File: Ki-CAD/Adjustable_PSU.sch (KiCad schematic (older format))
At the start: 12 parts, among them T1 TRANSFO4 - 50V

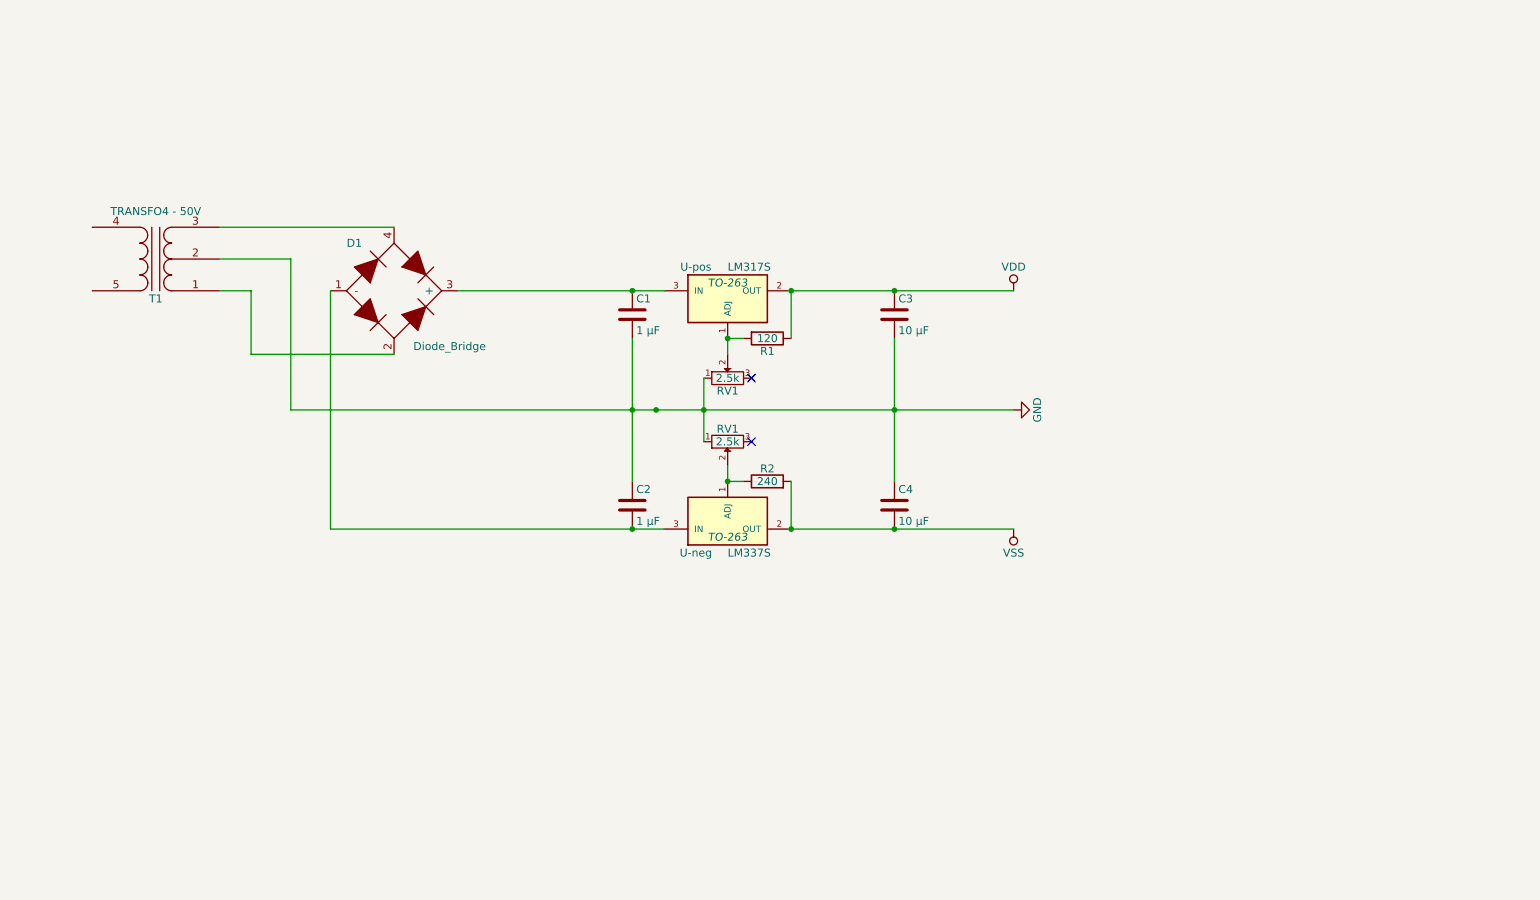
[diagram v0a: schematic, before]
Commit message: added 5v rail and new footprints (to be added to future personal kicad repo)
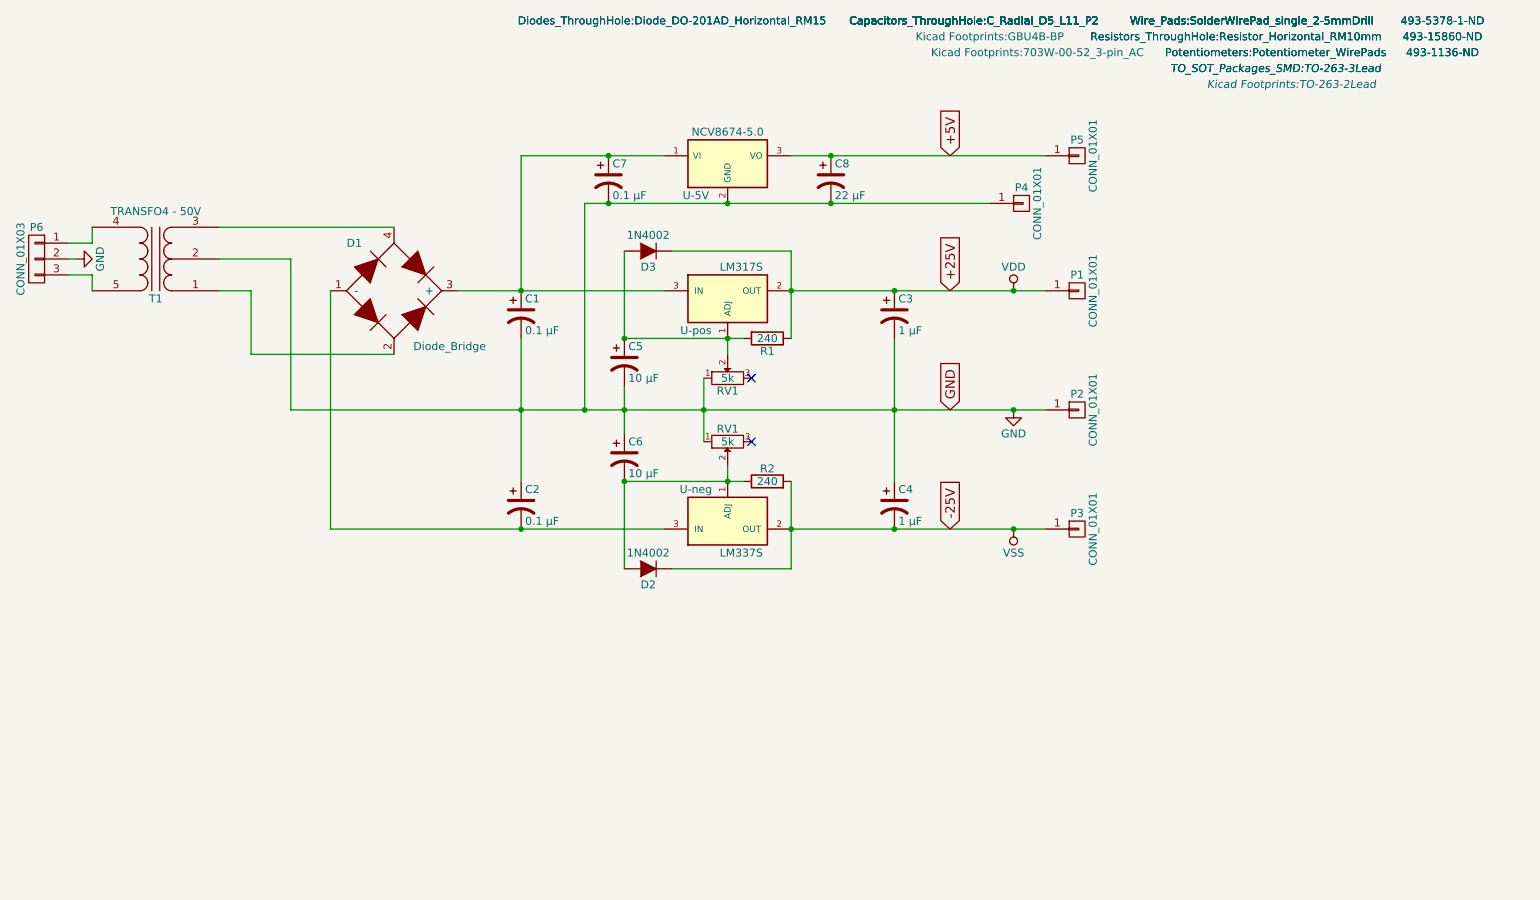
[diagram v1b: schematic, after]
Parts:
- removed C1, C2: 1 μF, symbol C
- removed C3, C4: 10 μF, symbol C
- added C1, C2, C7: 0.1 μF, Capacitors_ThroughHole:C_Radial_D5_L11_P2, symbol CP1
- added C3, C4: 1 μF, Capacitors_ThroughHole:C_Radial_D5_L11_P2, symbol CP1
- added C5, C6: 10 μF, Capacitors_ThroughHole:C_Radial_D5_L11_P2, symbol CP1
- added C8: 22 μF, Capacitors_ThroughHole:C_Radial_D5_L11_P2, symbol CP1
- added D2, D3: 1N4002, Diodes_ThroughHole:Diode_DO-201AD_Horizontal_RM15, symbol D
- added P1, P2, P3, P4, P5: CONN_01X01, Wire_Pads:SolderWirePad_single_2-5mmDrill, symbol CONN_01X01
- added P6: CONN_01X03, Kicad Footprints:703W-00-52_3-pin_AC, symbol CONN_01X03
- added U-5V: NCV8674-5.0, Kicad Footprints:TO-263-2Lead, symbol SPX2920T-5.0
- D1: footprint (none) -> Kicad Footprints:GBU4B-BP
- R1: value 120 -> 240; footprint (none) -> Resistors_ThroughHole:Resistor_Horizontal_RM10mm
- R2: footprint (none) -> Resistors_ThroughHole:Resistor_Horizontal_RM10mm
- RV1: value 2.5k -> 5k; footprint (none) -> Potentiometers:Potentiometer_WirePads
- U-neg, U-pos: footprint TO-263 -> TO_SOT_Packages_SMD:TO-263-3Lead
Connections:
- net GND: now also C1.2, C2.1, C3.2, C4.1, C5.2, C6.1, C7.2, C8.2, P2.1 (P1), P4.1 (P1), P6.2 (P2), U-5V.2 (GND)
- net VDD: now also C3.1, D3.1 (K), P1.1 (P1)
- net VSS: now also C4.2, D2.1 (K), P3.1 (P1)
- net at T1.4 (S1): now also P6.1 (P1)
- net at T1.5 (S2): now also P6.3 (P3)
- net at D1.1 (-), U-neg.3 (IN): now also C2.2
- net at D1.3 (+), U-pos.3 (IN): now also C1.1, C7.1, U-5V.1 (VI)
- net at R1.2, RV1.2, U-pos.1 (ADJ): now also C5.1, D3.2 (A)
- net at R2.1, RV1.2, U-neg.1 (ADJ): now also C6.2, D2.2 (A)
- new net +5V: C8.1, P5.1 (P1), U-5V.3 (VO)

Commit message: placed op-amps for cheesy integrator based function generator (square, ramp, "sine"
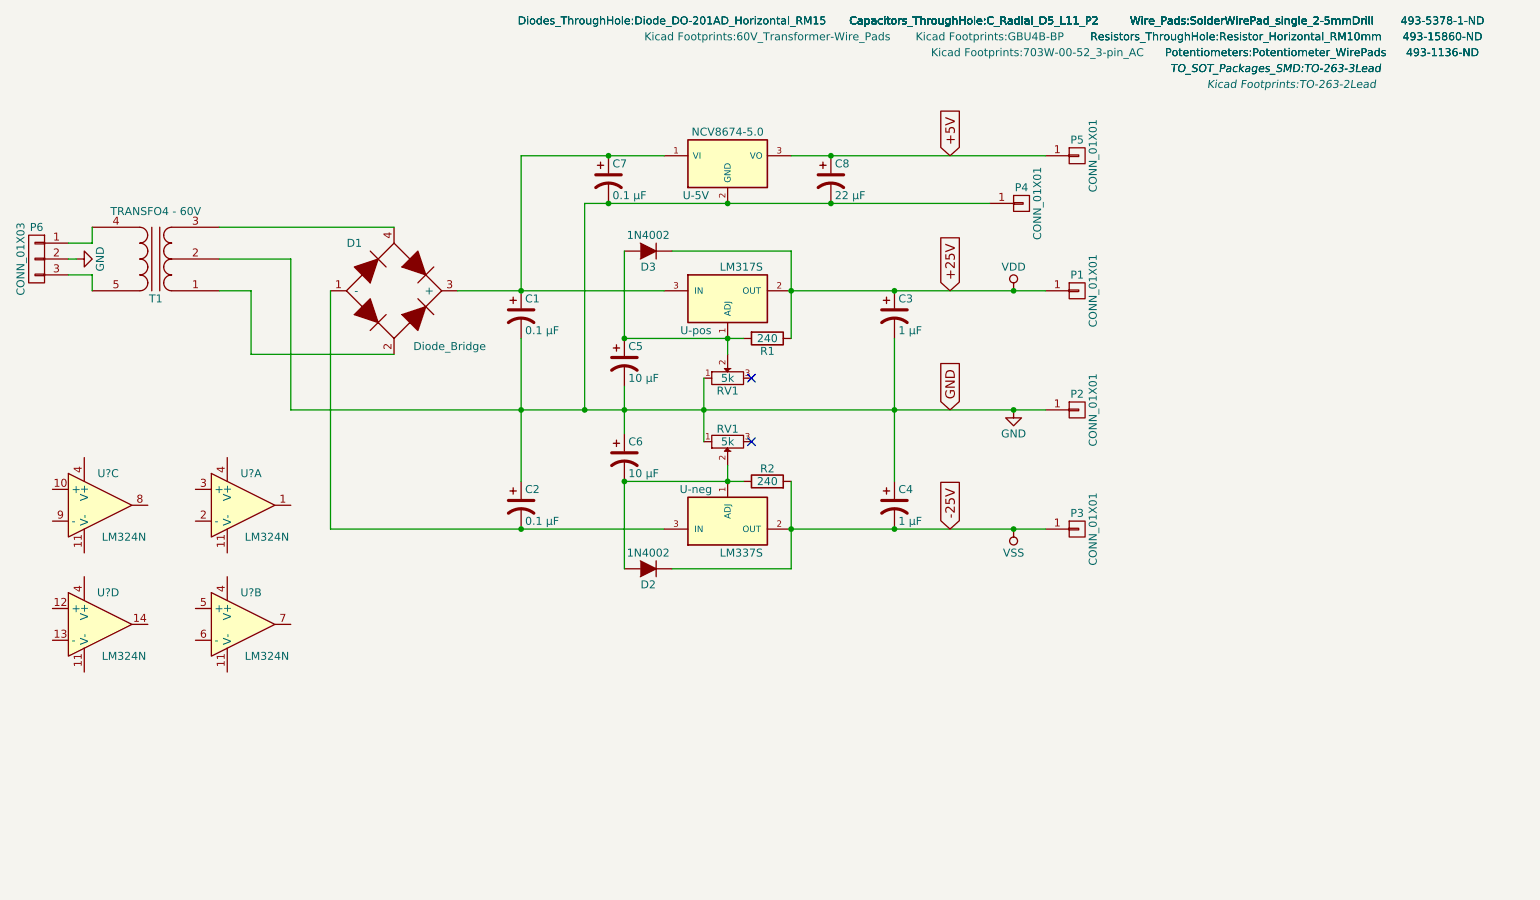
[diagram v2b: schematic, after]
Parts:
- added U? (x4): LM324N, symbol LM324N
- T1: value TRANSFO4 - 50V -> TRANSFO4 - 60V; footprint (none) -> Kicad Footprints:60V_Transformer-Wire_Pads
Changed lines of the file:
@@
 P 2750 2050
 F 0 "T1" H 2750 2300 50  0000 C CNN
-F 1 "TRANSFO4 - 50V" H 2750 1750 50  0000 C CNN
-F 2 "" H 2750 2050 50  0000 C CNN
+F 1 "TRANSFO4 - 60V" H 2750 1750 50  0000 C CNN
+F 2 "Kicad Footprints:60V_Transformer-Wire_Pads" H -1100 650 50  0000 C CNN
 F 3 "" H 2750 2050 50  0000 C CNN
 	1    2750 2050
@@
 	1    0    0    -1
 $EndComp
+$Comp
+L LM324N U?
+U 1 1 586DCD33
+P 3300 3600
+F 0 "U?" H 3350 3800 50  0000 C CNN
+F 1 "LM324N" H 3450 3400 50  0000 C CNN
+F 2 "" H 3250 3700 50  0000 C CNN
+F 3 "" H 3350 3800 50  0000 C CNN
+	1    3300 3600
+	1    0    0    -1
+$EndComp
+$Comp
+L LM324N U?
+U 2 1 586DCD90
+P 3300 4350
+F 0 "U?" H 3350 4550 50  0000 C CNN
+F 1 "LM324N" H 3450 4150 50  0000 C CNN
+F 2 "" H 3250 4450 50  0000 C CNN
+F 3 "" H 3350 4550 50  0000 C CNN
+	2    3300 4350
+	1    0    0    -1
+$EndComp
+$Comp
+L LM324N U?
+U 3 1 586DCE16
+P 2400 3600
+F 0 "U?" H 2450 3800 50  0000 C CNN
+F 1 "LM324N" H 2550 3400 50  0000 C CNN
+F 2 "" H 2350 3700 50  0000 C CNN
+F 3 "" H 2450 3800 50  0000 C CNN
+	3    2400 3600
+	1    0    0    -1
+$EndComp
+$Comp
+L LM324N U?
+U 4 1 586DCEAF
+P 2400 4350
+F 0 "U?" H 2450 4550 50  0000 C CNN
+F 1 "LM324N" H 2550 4150 50  0000 C CNN
+F 2 "" H 2350 4450 50  0000 C CNN
+F 3 "" H 2450 4550 50  0000 C CNN
+	4    2400 4350
+	1    0    0    -1
+$EndComp

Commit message: started board layout, changed gnd to earth-gnd
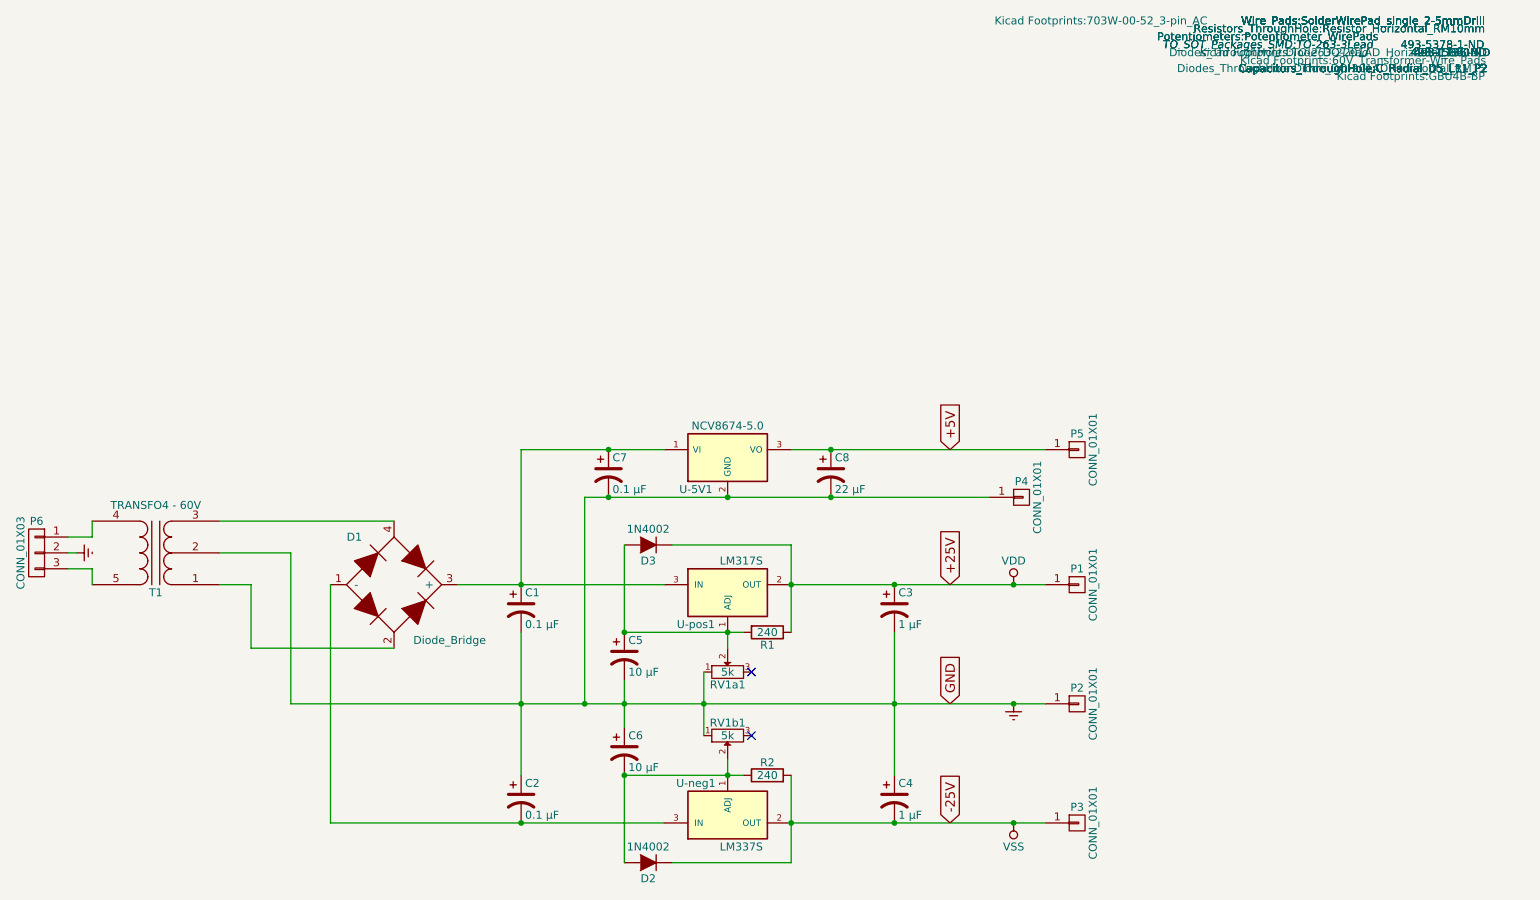
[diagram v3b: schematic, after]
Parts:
- removed U? (x4): LM324N, symbol LM324N
- renumbered RV1 to RV1a1, RV1 to RV1b1, U-5V to U-5V1, U-neg to U-neg1, U-pos to U-pos1
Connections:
- net GND renamed Earth
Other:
- moved on the sheet: C1, C2, C3, C4, C5, C6, C7, C8, D1, D2, D3, P1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
